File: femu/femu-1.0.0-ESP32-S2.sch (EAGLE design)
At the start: 54 parts, among them IC1 ESP32-QFN_5X5

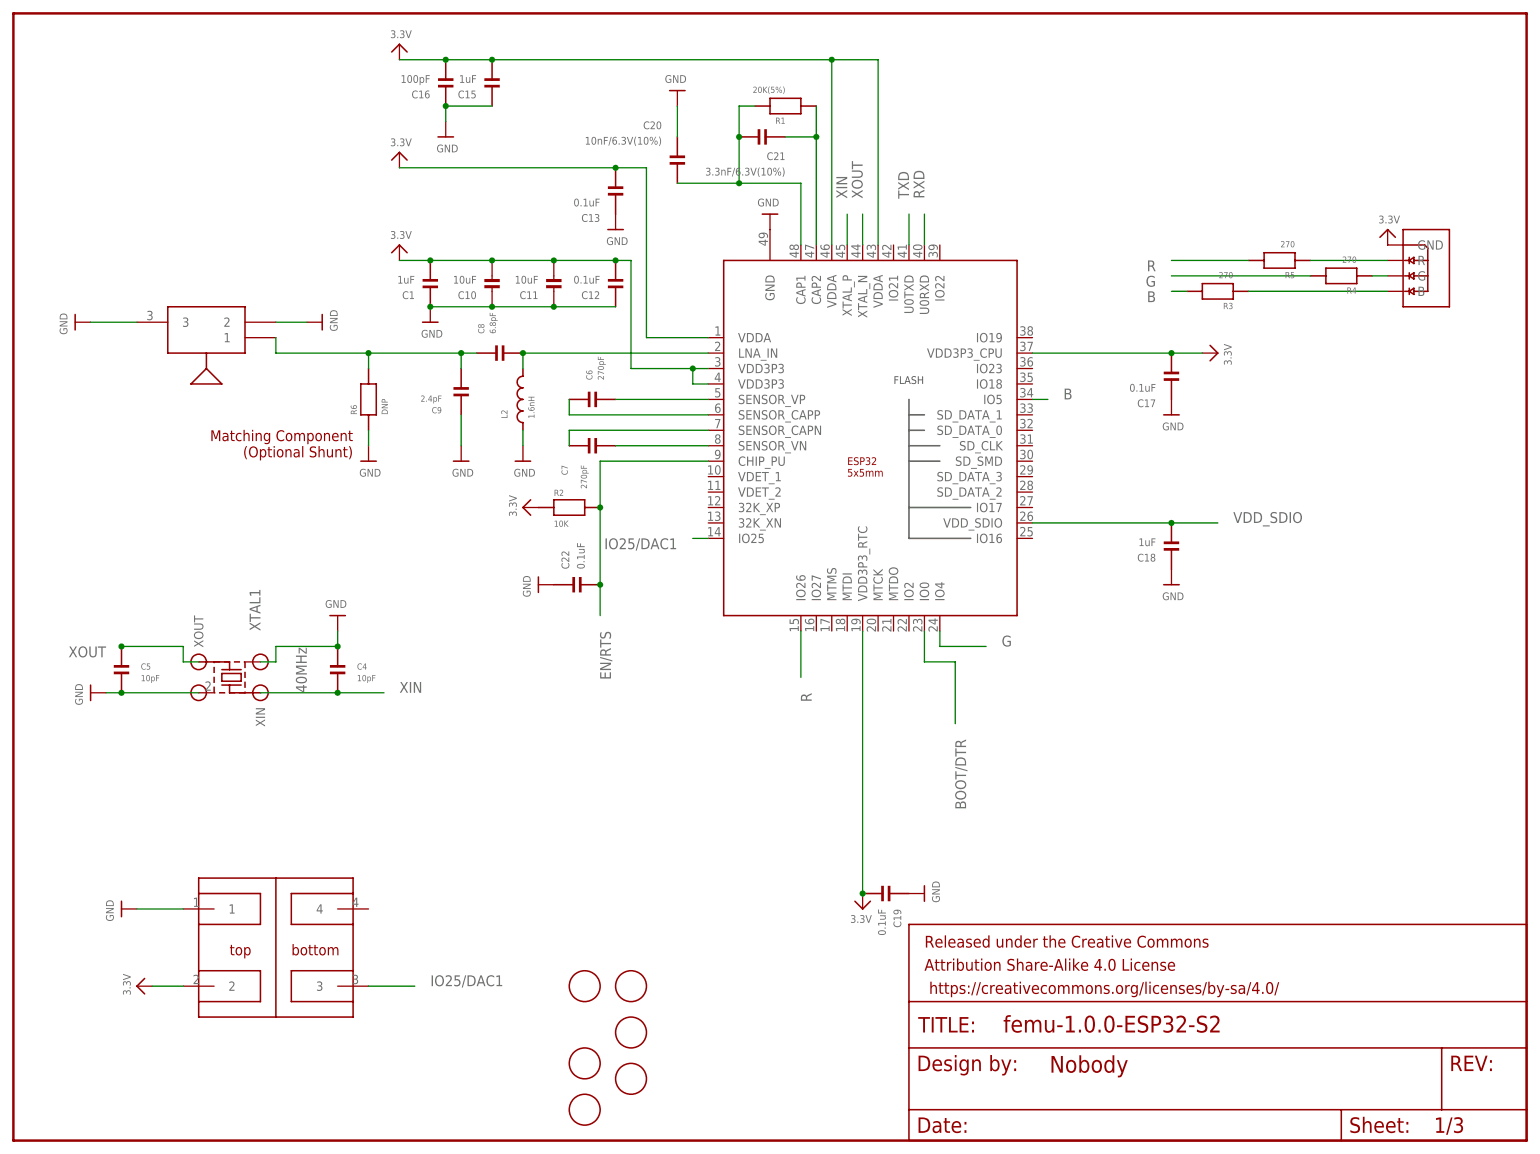
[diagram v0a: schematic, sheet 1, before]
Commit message: Adding work on femu 1.0.2, and 1.0.3
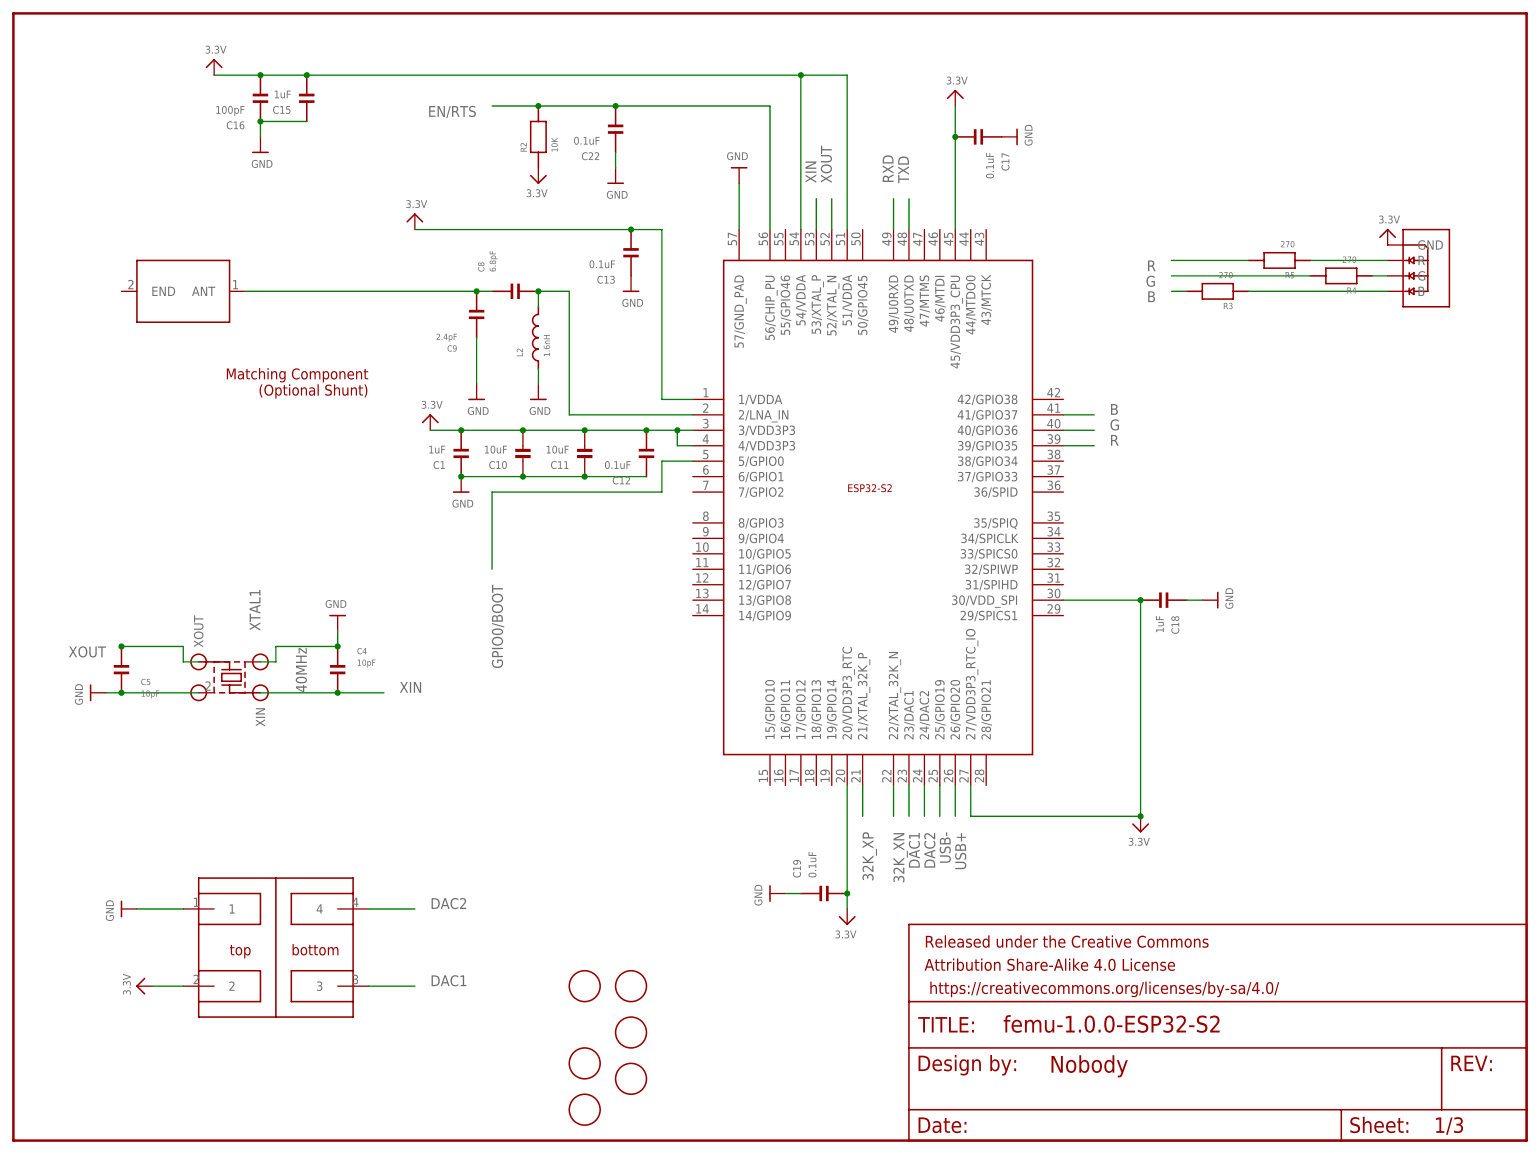
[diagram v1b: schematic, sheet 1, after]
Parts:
- removed ANT1: PULSE_ANT_2.4GHZ, bar_antenna:PULSE_ANT_2.4GHZ
- removed C20: 10nF/6.3V(10%), parts_01005:CAPACITOR
- removed C21: 3.3nF/6.3V(10%), parts_0201:CAPACITOR_0201
- removed C23: 4.7uF, parts_0201:CAPACITOR_0201
- removed C25, C27: 0.1uF, parts_0201:CAPACITOR_0201
- removed C6, C7: 270pF, parts_0201:CAPACITOR_0201
- removed IC1: ESP32-QFN_5X5, esp32-wroom-32:ESP32-QFN_5X5
- removed R1: 20K(5%), parts_01005:RESISTOR
- removed R6: DNP, parts_0201:RESISTOR_0201
- removed U$11: FT231XQ, ftdi_ft231x:FT231XQ
- added U$10: AF216M245001-T, taydo-yuden-rf-antenna:AF216M245001-T
- added U$38: ESP32-S2_7X7, esp32-wroom-32:ESP32-S2_7X7
- C12: device parts_0201:CAPACITOR_0201 -> parts_01005:CAPACITOR; MPN GRM033C80J104KE84D -> GRM022R60G104ME15L
- C16: device parts_0201:CAPACITOR_0201 -> parts_01005:CAPACITOR; MPN 0201YC101KAT2A -> GRM0225C1E101GA02L
- C19, C22: device parts_0201:CAPACITOR_0201 -> parts_01005:CAPACITOR
- C2, C3: MPN 0201ZD105MAT2A -> CL03A105KQ3CSNH
- C4, C5: device parts_0201:CAPACITOR_0201 -> parts_01005:CAPACITOR; MPN CC0201JRNPO9BN100 -> GRM0225C1C100JA03L
- C8: device parts_0201:CAPACITOR_0201 -> parts_01005:CAPACITOR; MPN GRM0335C2A6R8DA01D -> GRM0225C1E6R8DA03L
- C9: device parts_0201:CAPACITOR_0201 -> parts_01005:CAPACITOR; MPN GRM0335C1H2R4CA01D -> GRM0225C1E2R4BA03L
- L2: device parts_0201:INDUCTOR_FIXED_0201 -> parts_01005:INDUCTOR; MPN LQP03HQ1N6B02D -> LQP02HQ1N6B02L
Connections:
- removed net BOOT/DTR: IC1.IO0, U$11.DTR
- removed net IO25/DAC1: IC1.IO25, U$6.3
- removed net N$1: C6.P$1, IC1.SENSOR_VP
- removed net N$2: C6.P$2, IC1.SENSOR_CAPP
- removed net N$3: C7.P$2, IC1.SENSOR_VN
- removed net N$4: C7.P$1, IC1.SENSOR_CAPN
- removed net N$7: C21.P$2, IC1.CAP2, R1.1
- removed net N$9: C20.P$2, C21.P$1, IC1.CAP1, R1.2
- removed net VDD_SDIO: C18.P$2, IC1.VDD_SDIO
- new net 32K_XN: U$38.22/XTAL_32K_N
- new net 32K_XP: U$38.21/XTAL_32K_P
- new net DAC1: U$38.23/DAC1, U$6.3
- new net DAC2: U$38.24/DAC2, U$6.4
- new net GPIO0/BOOT: U$38.5/GPIO0
- new net N$11: C13.P$2, U$38.1/VDDA@1
- new net N$13: C1.P$2, C10.P$2, C11.P$2, C12.P$2, U$38.3/VDD3P3@1, U$38.4/VDD3P3@2
- net 3.3V: now also C18.P$2, U$38.20/VDD3P3_RTC, U$38.27/VDD3P3_RTC_IO, U$38.30/VDD_SPI, U$38.45/VDD3P3_CPU, U$38.51/VDDA@2, U$38.54/VDDA@3; no longer C1.P$2, C10.P$2, C11.P$2, C12.P$2, C13.P$2, C25.P$2, IC1.VDD3P3@1, IC1.VDD3P3@2, IC1.VDD3P3_CPU, IC1.VDD3P3_RTC, IC1.VDDA@1, IC1.VDDA@2, IC1.VDDA@3, U$11.3V3OUT, U$11.RESET#, U$11.VCCIO
- net ANT: now also U$38.2/LNA_IN; no longer IC1.LNA_IN
- net B: now also U$38.41/GPIO37; no longer IC1.IO5
- net EN/RTS: now also U$38.56/CHIP_PU; no longer IC1.CHIP_PU, U$11.RTS
- net G: now also U$38.40/GPIO36; no longer IC1.IO4
- net GND: now also U$38.57/GND_PAD; no longer ANT1.2, ANT1.3, C20.P$1, C23.P$1, C25.P$1, C27.P$1, IC1.GND, R6.1, U$11.GND@13, U$11.GND@21, U$11.GND@3
- net N$6: now also U$10.ANT; no longer ANT1.1, R6.2
- net R: now also U$38.39/GPIO35; no longer IC1.IO26
- net RXD: now also U$38.49/U0RXD; no longer IC1.U0RXD, U$11.TXD
- net TXD: now also U$38.48/U0TXD; no longer IC1.U0TXD, U$11.RXD
- net USB+: now also U$38.26/GPIO20; no longer U$11.USBDP
- net USB-: now also U$38.25/GPIO19; no longer U$11.USBDM
- net VIN: no longer C23.P$2, C27.P$2, U$11.VCC
- net XIN: now also U$38.53/XTAL_P; no longer IC1.XTAL_P
- net XOUT: now also U$38.52/XTAL_N; no longer IC1.XTAL_N
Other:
- note added: "COMMS - USB HID"
- note removed: "COMMS - FTDI USB to UART, USB HID"
- moved on the sheet: C1, C10, C11, C12, C13, C15, C16, C17, C18, C19, C22, C8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

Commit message: Adding current work on FEMU v1.0.3, which includes microvia adjustments
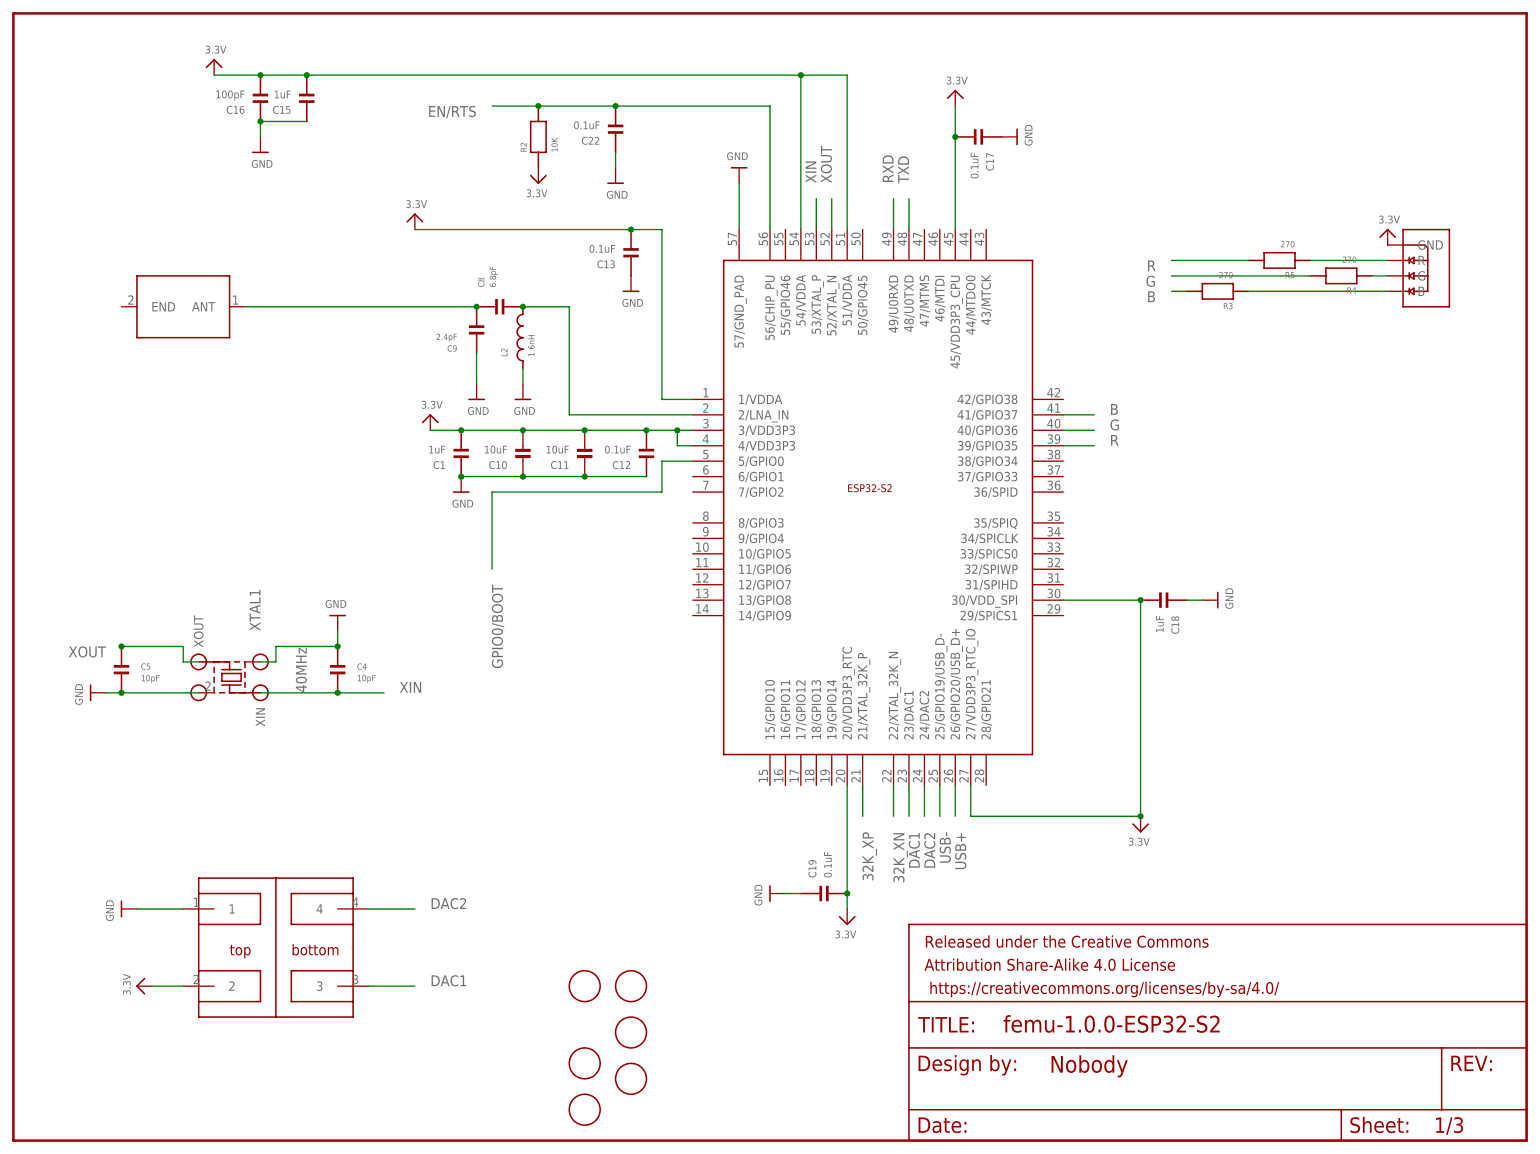
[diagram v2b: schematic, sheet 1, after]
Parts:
- added FB2: (no value), microbuilder:FERRITE_0402MP
- C12, C13, C16, C17, C19, C22, C4, C5, C8, C9: device parts_01005:CAPACITOR -> parts_0201:CAPACITOR_0201
- L2: device parts_01005:INDUCTOR -> parts_0201:INDUCTOR_FIXED_0201
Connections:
- new net N$1: FB2.P$1, U$37.GND
- net GND: now also FB2.P$2; no longer U$37.GND
- net USB+: now also U$38.26/GPIO20/USB_D+; no longer U$38.26/GPIO20
- net USB-: now also U$38.25/GPIO19/USB_D-; no longer U$38.25/GPIO19
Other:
- note removed: "Matching Component (Optional Shunt)"
- moved on the sheet: C8, C9, L2
